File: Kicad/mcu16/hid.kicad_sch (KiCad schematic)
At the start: 26 parts, among them IC401 MCP2221A, K401 FRONT #1, K402 FRONT #2, K403 VIN, K404 +5V, K405 FRONT #3, K406 SERVO LEFT, K407 USB/UART, K408 SERVO RIGHT

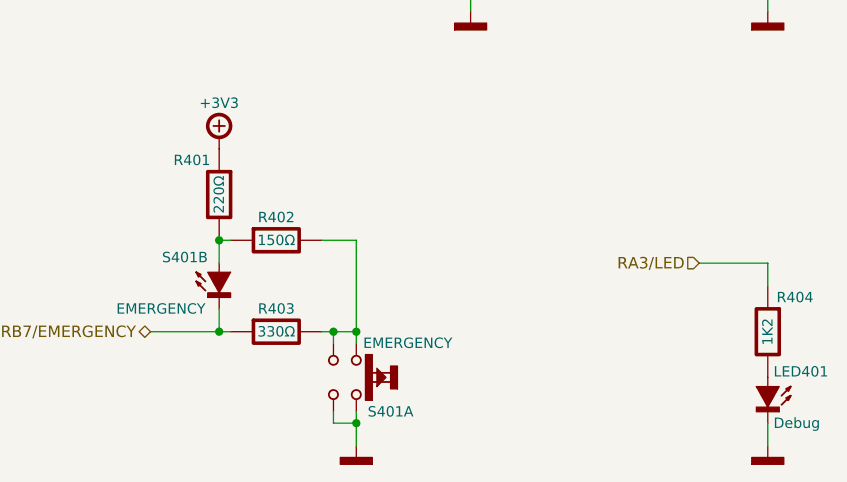
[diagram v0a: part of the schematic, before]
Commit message: Update hid.kicad_sch
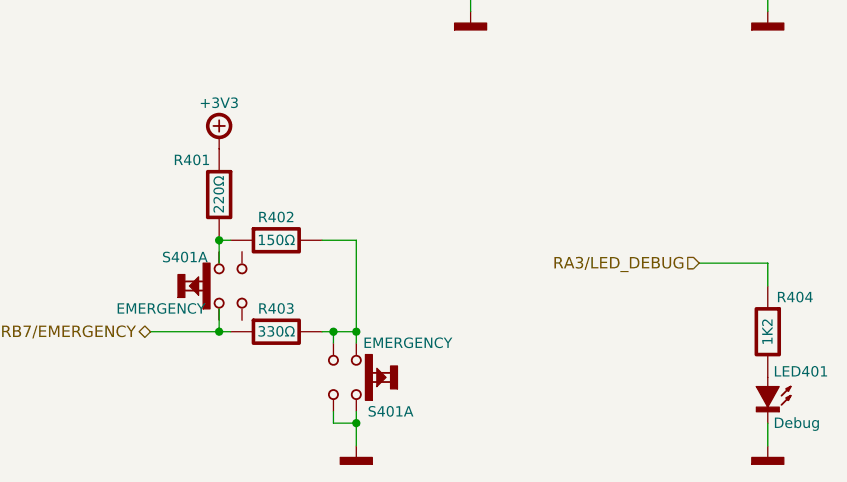
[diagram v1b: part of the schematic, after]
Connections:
- net RB7/EMERGENCY: no longer S401.5 (C)
- net at R401.1, R402.2: no longer S401.6 (A)
- net RA3/LED renamed RA3/LED_DEBUG

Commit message: Draft
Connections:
- net RB7/EMERGENCY: now also S401.5 (C)
- net at R401.1, R402.2: now also S401.6 (A)
